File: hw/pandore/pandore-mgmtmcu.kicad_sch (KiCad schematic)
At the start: 0 parts

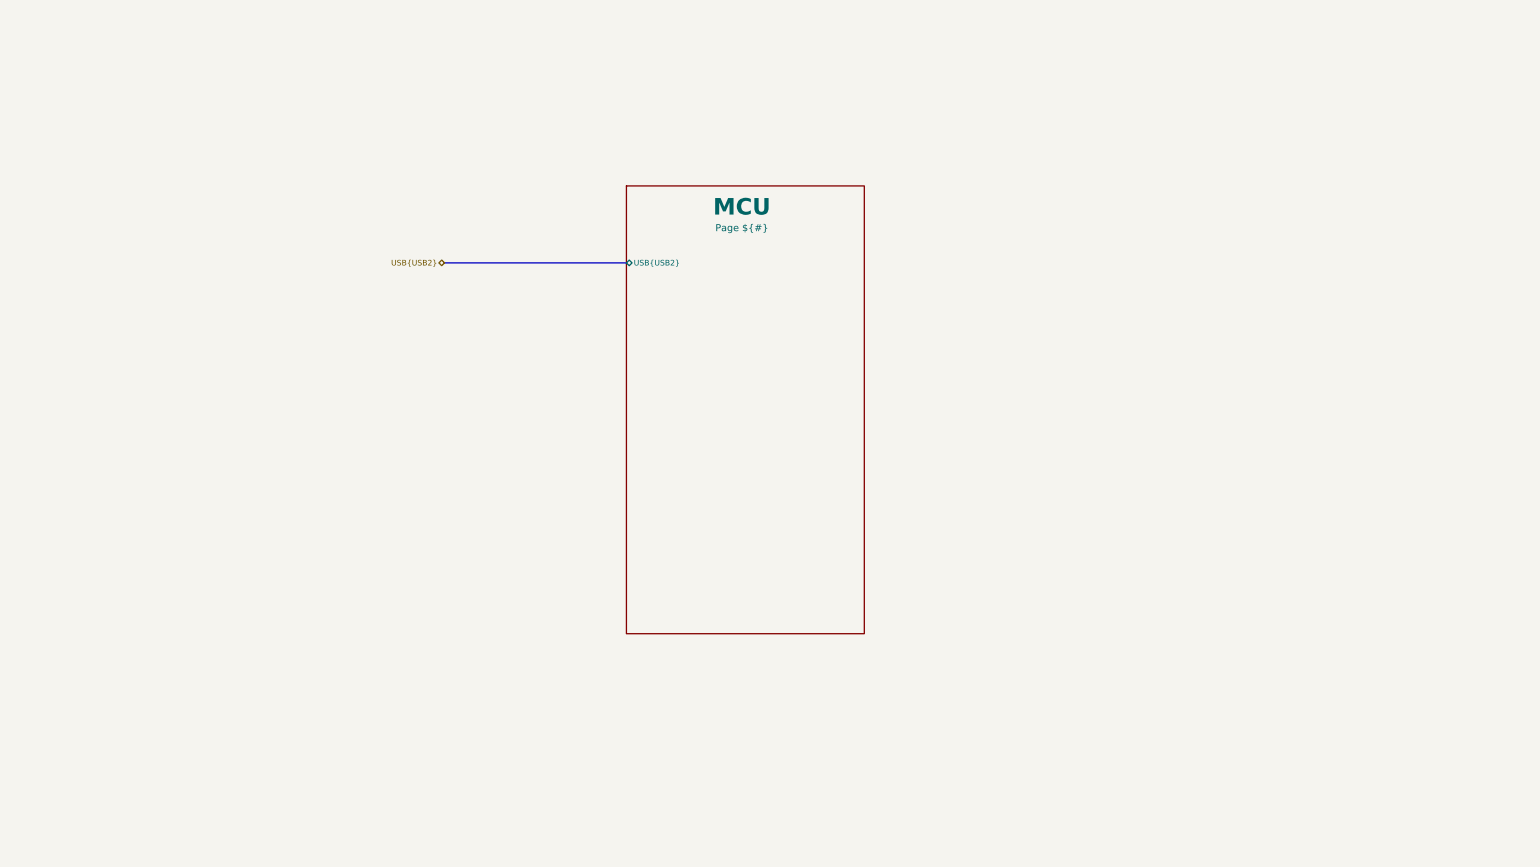
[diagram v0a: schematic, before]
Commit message: Added lots to sch and pcb: eth passive, audio codec, midi, teensy Corrected and added support for M.2
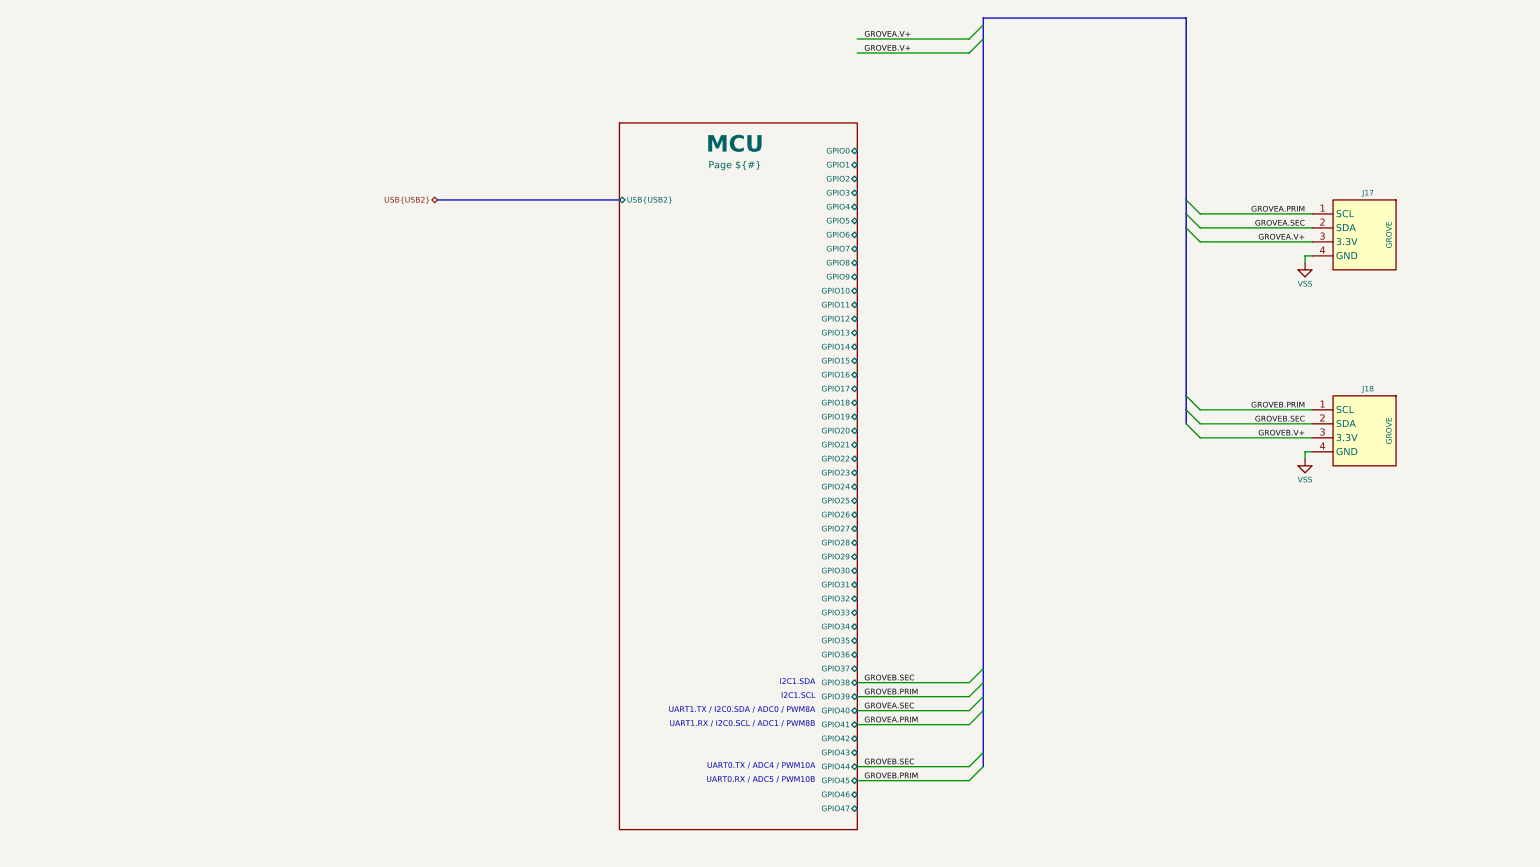
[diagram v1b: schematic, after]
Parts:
- added J17, J18: GROVE, reekilib_con:te_2041145-4, symbol reekilib_con:grove
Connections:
- new net GROVEA.PRIM: J17.1 (D0)
- new net GROVEA.SEC: J17.2 (D1)
- new net GROVEA.V+: J17.3 (3.3V)
- new net GROVEB.PRIM: J18.1 (D0)
- new net GROVEB.SEC: J18.2 (D1)
- new net GROVEB.V+: J18.3 (3.3V)
- new net VSS: J17.4 (GND), J18.4 (GND)
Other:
- sheet MCU ports: added GPIO0, GPIO1, GPIO10, GPIO11, GPIO12, GPIO13, GPIO14, GPIO15, GPIO16, GPIO17, GPIO18, GPIO19, GPIO2, GPIO20, GPIO21, GPIO22, GPIO23, GPIO24, GPIO25, GPIO26, GPIO27, GPIO28, GPIO29, GPIO3, GPIO30, GPIO31, GPIO32, GPIO33, GPIO34, GPIO35, GPIO36, GPIO37, GPIO38, GPIO39, GPIO4, GPIO40, GPIO41, GPIO42, GPIO43, GPIO44, GPIO45, GPIO46, GPIO47, GPIO5, GPIO6, GPIO7, GPIO8, GPIO9; removed none
- note added: "I2C1.SCL"
- note added: "I2C1.SDA"
- note added: "UART0.RX / ADC5 / PWM10B"
- note added: "UART0.TX / ADC4 / PWM10A"
- note added: "UART1.RX / I2C0.SCL / ADC1 / PWM8B"
- note added: "UART1.TX / I2C0.SDA / ADC0 / PWM8A"

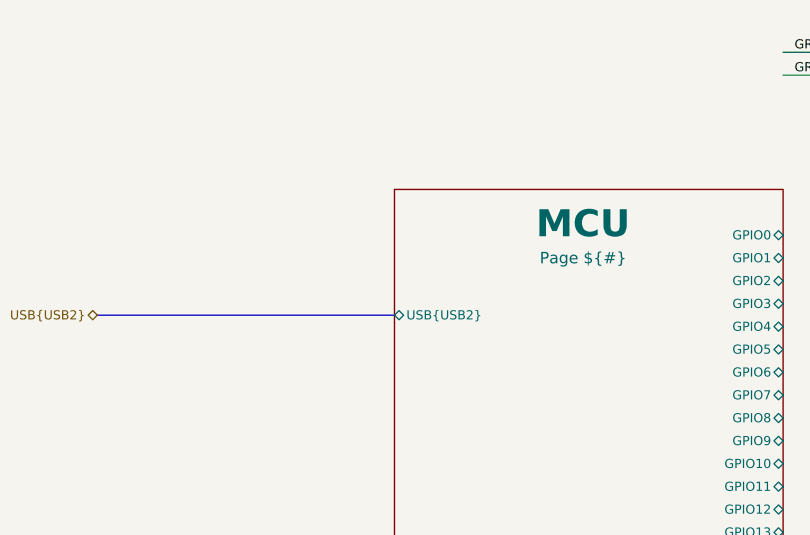
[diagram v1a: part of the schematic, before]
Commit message: Lots of routing done power blocks intra-routing mostly done rp2350 routing mostly done some label cleanup
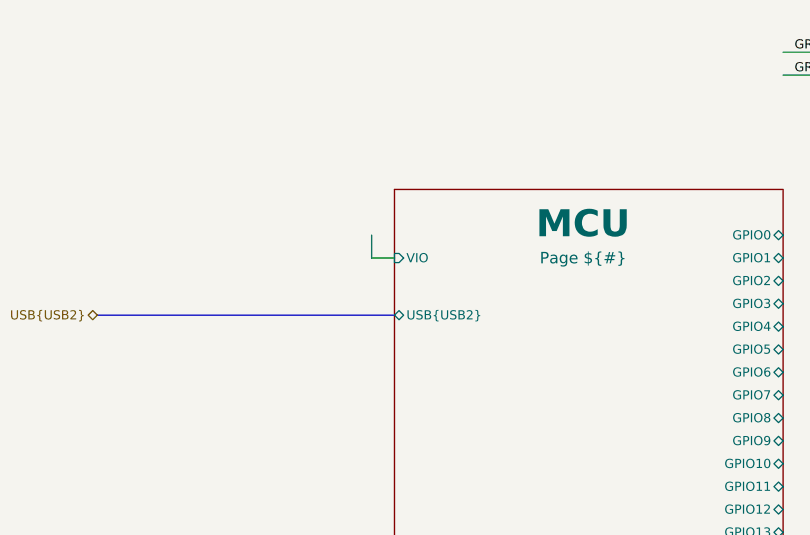
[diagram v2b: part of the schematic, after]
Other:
- sheet MCU ports: added VIO; removed none
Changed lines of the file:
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@@
+	(wire
+		(pts
+			(xy 111.76 55.88) (xy 111.76 58.42)
+		)
+		(stroke
+			(width 0)
+			(type default)
+		)
+	)
 	(wire
 		(pts
@@
 		(pts
 			(xy 238.76 110.49) (xy 238.76 111.76)
+		)
+		(stroke
+			(width 0)
+			(type default)
+		)
+	)
+	(wire
+		(pts
+			(xy 114.3 58.42) (xy 111.76 58.42)
 		)
 		(stroke
@@
 			)
 		)
+		(pin "VIO" input
+			(at 114.3 58.42 180)
+			(effects
+				(font
+					(size 1.016 1.016)
+				)
+				(justify left)
+			)
+		)

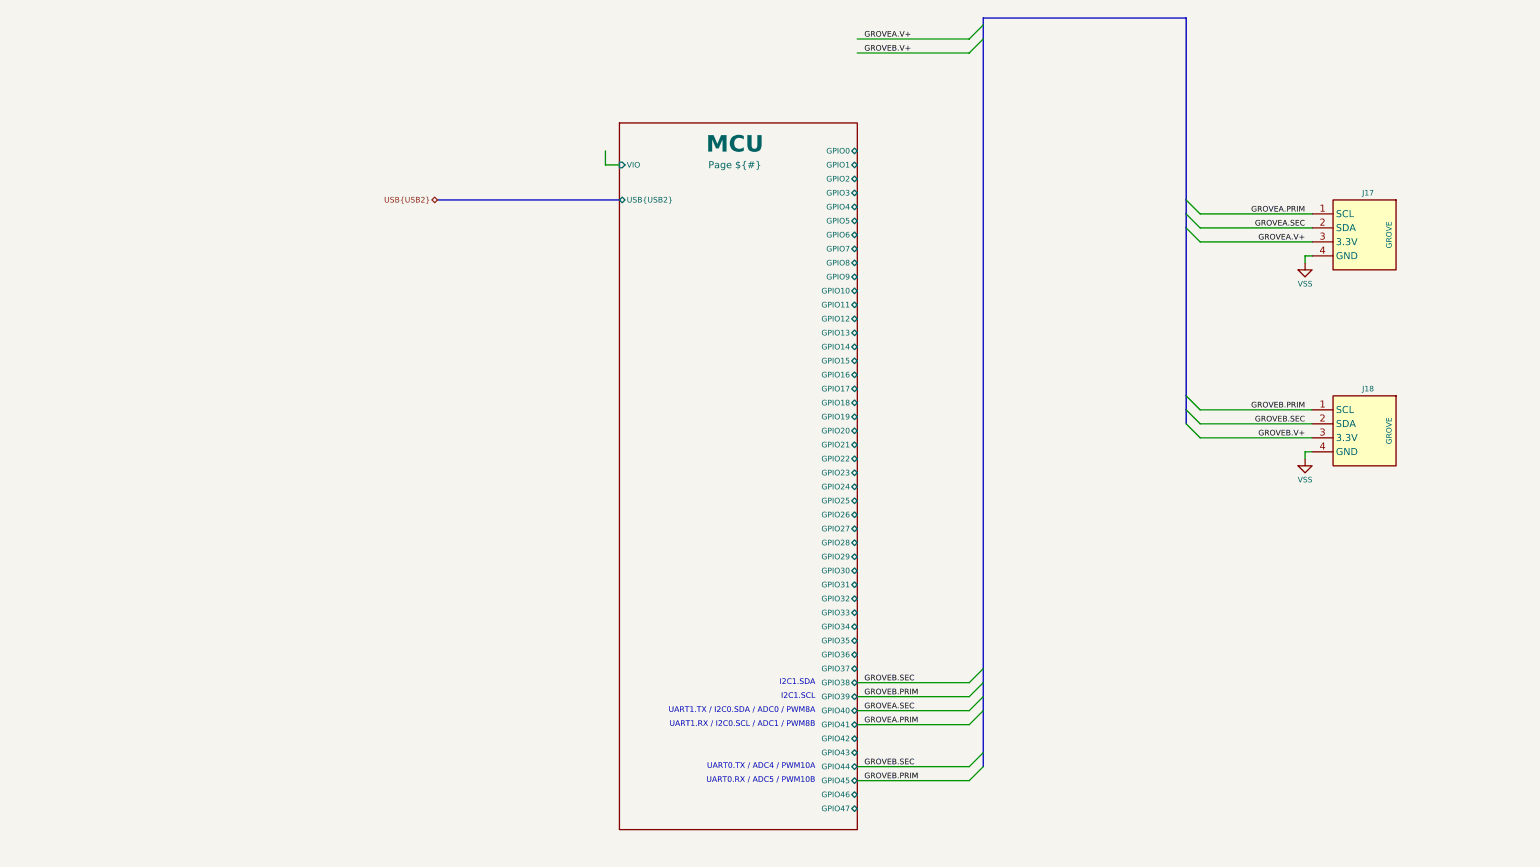
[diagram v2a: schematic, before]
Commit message: added encoder, more routing done, pinout doc added
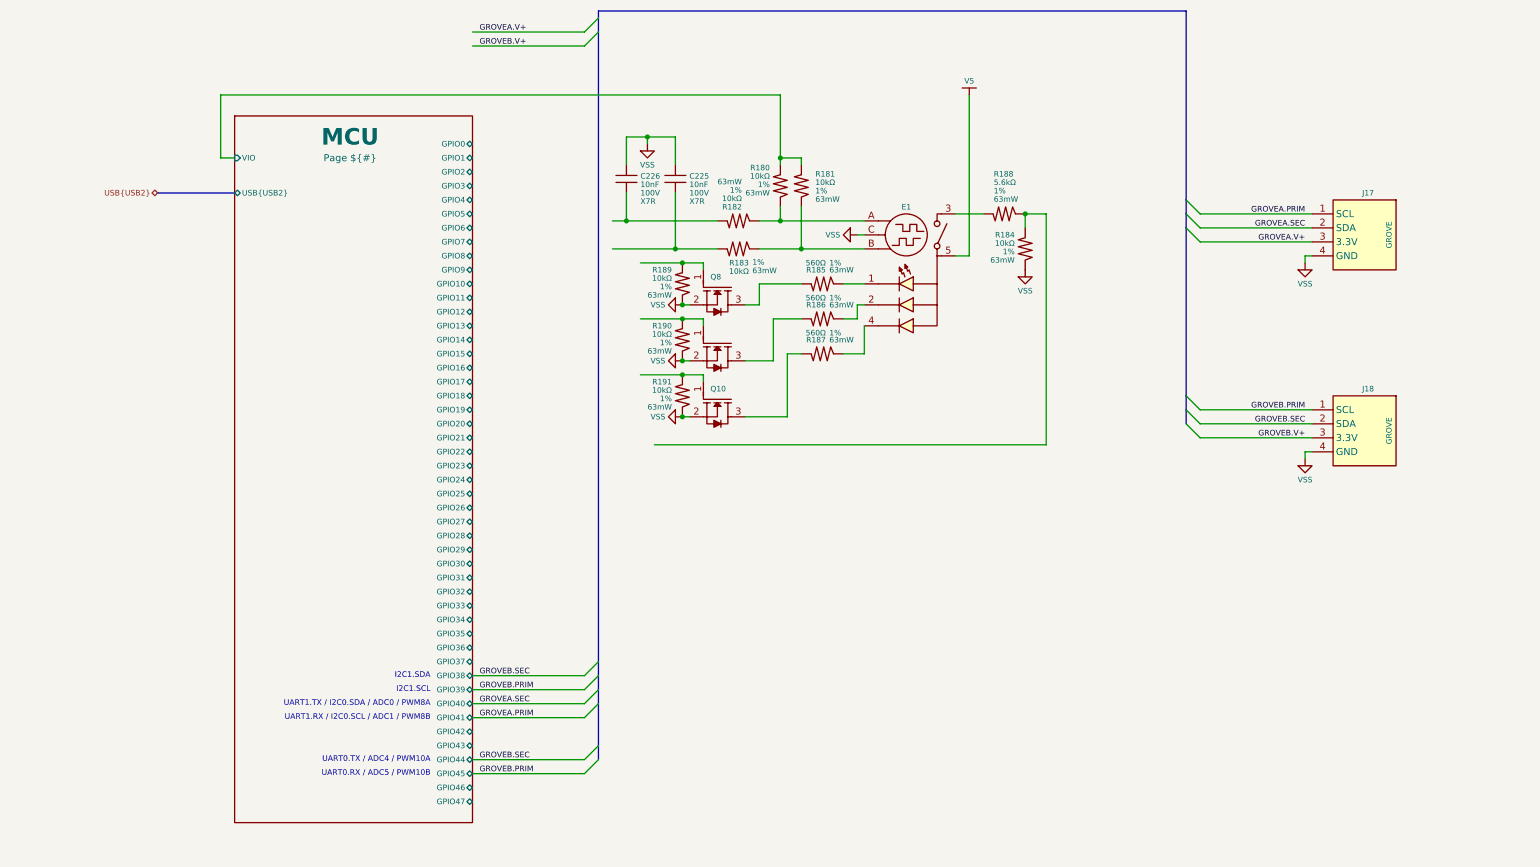
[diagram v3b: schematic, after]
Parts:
- added C225, C226: ${Capacitance}, ${Voltage}, ${Dielectric}, reekilib_cap:CAPC1608, symbol reekilib_cap:cap
- added E1: 24p + sw + rgb, reekilib_enc:bourns_PEL12T-4xxxx-S, symbol reekilib_enc:enc_rot_btn_rgb
- added Q10, Q8, Q9: MOSFET_EN-N, reekilib_sot:SOT95P280X100-3, symbol reekilib_mfe:MOSFET_EN-N
- added R180, R181, R182, R183, R184, R185, R186, R187, R188, R189, R190, R191: ${Resistance}, ${Tolerance}, ${Power}, reekilib_res:RESC1005, symbol reekilib_res:res
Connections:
- net MCU/VIO: now also R180.1, R181.1
- net VSS: now also C225.2, C226.2, E1.C (EC), Q10.2 (S), Q8.2 (S), Q9.2 (S), R184.2, R189.2, R190.2, R191.2
- new net: Q10.3 (D), R187.1
- new net: E1.4 (LB), R187.2
- new net: E1.A (EA), R180.2, R182.2
- new net: Q8.3 (D), R185.1
- new net: E1.1 (LR), R185.2
- new net: Q9.1 (G), R190.1
- new net: Q9.3 (D), R186.1
- new net: E1.2 (LG), R186.2
- new net: Q8.1 (G), R189.1
- new net: C226.1, R182.1
- new net: C225.1, R183.1
- new net: E1.B (EB), R181.2, R183.2
- new net: Q10.1 (G), R191.1
- new net: E1.3 (SO), R188.1
- new net: R184.1, R188.2
- new net V5: E1.5 (CM)

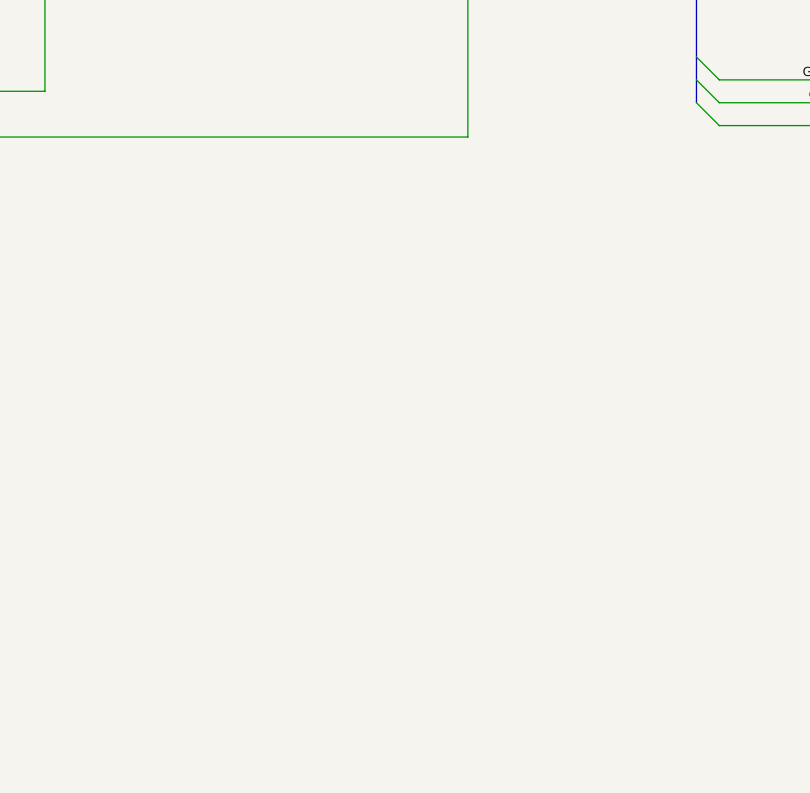
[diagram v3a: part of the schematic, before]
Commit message: added display flatflex conn
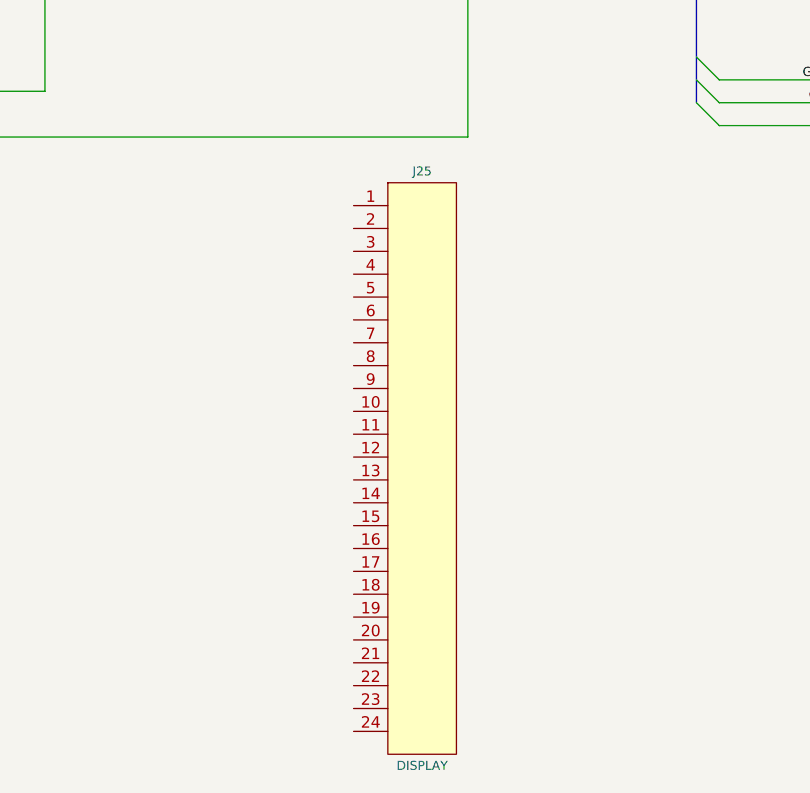
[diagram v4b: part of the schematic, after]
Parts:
- added J25: DISPLAY, reekilib_con:gct_FFC2A32-xx-T, symbol reekilib_con:hdr-1x24
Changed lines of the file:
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@@
+	)
+	(symbol
+		(lib_id "reekilib_con:hdr-1x24")
+		(at 186.69 146.05 0)
+		(unit 1)
+		(exclude_from_sim yes)
+		(in_bom yes)
+		(on_board yes)
+		(dnp no)
+		(fields_autoplaced yes)
+		(property "Reference" "J25"
+			(at 186.69 113.03 0)
+			(do_not_autoplace yes)
+			(effects
+				(font
+					(size 1 1)
+				)
+			)
+		)
+		(property "Value" "DISPLAY"
+			(at 186.69 179.07 0)
+			(do_not_autoplace yes)
+			(effects
+				(font
+					(size 1 1)
+				)
+			)
+		)
+		(property "Footprint" "reekilib_con:gct_FFC2A32-xx-T"
+			(at 186.69 182.118 0)
+			(do_not_autoplace yes)
+			(effects
+				(font
+					(size 1 1)
+				)
+				(hide yes)
+			)
+		)
+		(property "Datasheet" "https://gct.co/files/drawings/ffc2a32.pdf"
+			(at 186.69 186.436 0)
+			(do_not_autoplace yes)
+			(effects
+				(font
+					(size 1 1)
+				)
+				(hide yes)
+			)
+		)
+		(property "Description" "header 1row 24pin"
+			(at 186.69 183.642 0)
+			(do_not_autoplace yes)
+			(effects
+				(font
+					(size 1 1)
+				)
+				(hide yes)
+			)
+		)
+		(property "MPN" "FFC2A32-24-T"
+			(at 186.69 180.594 0)
+			(do_not_autoplace yes)
+			(effects
+				(font
+					(size 1 1)
+				)
+				(hide yes)
+			)
+		)
+		(property "MFG" "GCT"
+			(at 193.294 180.594 0)
+			(do_not_autoplace yes)
+			(effects
+				(font
+					(size 1 1)
+				)
+				(justify left)
+				(hide yes)
+			)
+		)
+		(property "Link" "https://gct.co/connector/ffc2a32"
+			(at 186.69 185.166 0)
+			(do_not_autoplace yes)
+			(effects
+				(font
+					(size 1 1)
+				)
+				(hide yes)
+			)
+		)
+		(pin "9"
+		)
+		(pin "15"
+		)
+		(pin "16"
+		)
+		(pin "19"
+		)
+		(pin "10"
+		)
+		(pin "20"
+		)
+		(pin "21"
+		)
+		(pin "11"
+		)
+		(pin "17"
+		)
+		(pin "22"
+		)
+		(pin "2"
+		)
+		(pin "8"
+		)
+		(pin "18"
+		)
+		(pin "4"
+		)
+		(pin "5"
+		)
+		(pin "7"
+		)
+		(pin "6"
+		)
+		(pin "23"
+		)
+		(pin "24"
+		)
+		(pin "12"
+		)
+		(pin "14"
+		)
+		(pin "13"
+		)
+		(pin "1"
+		)
+		(pin "3"
+		)
+		(instances
+			(project ""
+				(path "/e55f2700-f75a-4062-8a27-fe258faa8966/57ec90ce-deb5-4a52-b1c0-0a997012959b"
+					(reference "J25")
+					(unit 1)
+				)
+			)
+		)
 	)
 	(symbol

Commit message: corrected display conn footprint
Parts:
- J25: footprint reekilib_con:gct_FFC2A32-xx-T -> reekilib_con:gct_FFC2A32-24-T
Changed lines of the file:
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@@
 			)
 		)
-		(property "Footprint" "reekilib_con:gct_FFC2A32-xx-T"
+		(property "Footprint" "reekilib_con:gct_FFC2A32-24-T"
 			(at 186.69 182.118 0)
 			(do_not_autoplace yes)
